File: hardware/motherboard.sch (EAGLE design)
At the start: 66 parts, among them IC1 7805T, Q1 16MHz, U1 ATMEGA328P-PU, U2 L293NE, U3 QRE1113, U4 QRE1113, U5 QRE1113, U6 QRE1113, U7 QRE1113, U8 QRE1113, U9 QRE1113

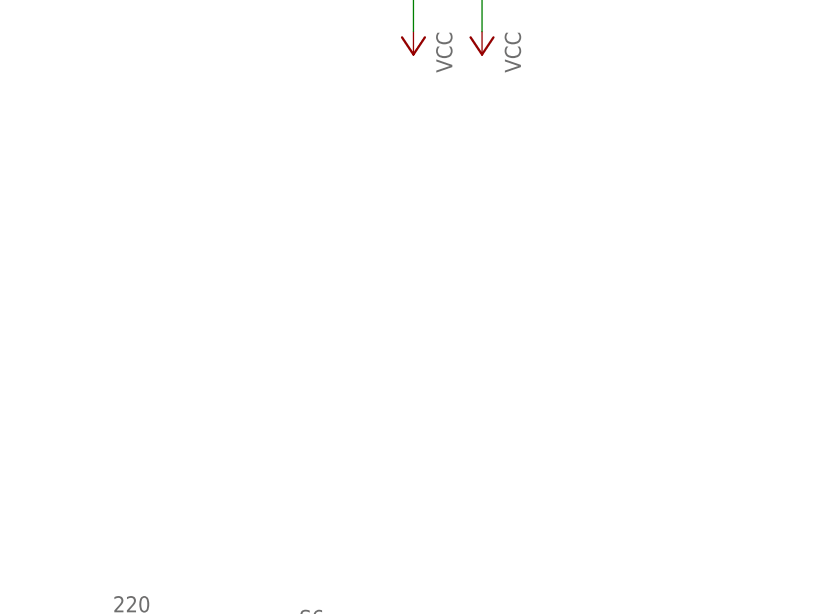
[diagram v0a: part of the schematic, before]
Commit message: Added a new board wich contains sensors.
Modified motherboard and removed sensors. Moved them to a new separate
board.
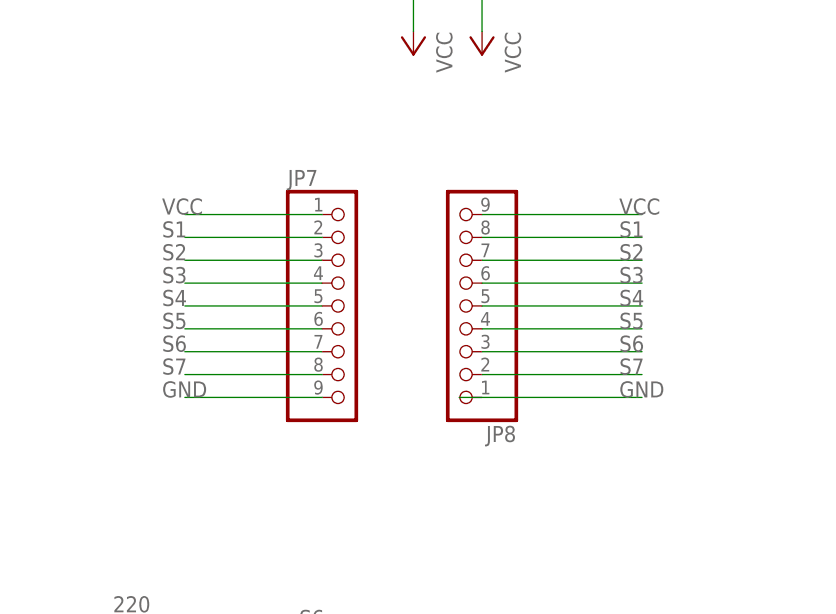
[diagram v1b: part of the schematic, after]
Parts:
- added JP7, JP8: (no value), pinhead:PINHD-1X9
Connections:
- net GND: now also JP7.9
- net S1: now also JP7.2, JP8.8
- net S2: now also JP7.3, JP8.7
- net S3: now also JP7.4, JP8.6
- net S4: now also JP7.5, JP8.5
- net S5: now also JP7.6, JP8.4
- net S6: now also JP7.7, JP8.3
- net S7: now also JP7.8, JP8.2
- net VCC: now also JP7.1, JP8.9
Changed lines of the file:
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@@
 <layers>
 <layer number="1" name="Top" color="4" fill="1" visible="no" active="no"/>
+<layer number="2" name="Route2" color="1" fill="3" visible="no" active="no"/>
+<layer number="3" name="Route3" color="4" fill="3" visible="no" active="no"/>
+<layer number="4" name="Route4" color="1" fill="4" visible="no" active="no"/>
+<layer number="5" name="Route5" color="4" fill="4" visible="no" active="no"/>
+<layer number="6" name="Route6" color="1" fill="8" visible="no" active="no"/>
+<layer number="7" name="Route7" color="4" fill="8" visible="no" active="no"/>
+<layer number="8" name="Route8" color="1" fill="2" visible="no" active="no"/>
+<layer number="9" name="Route9" color="4" fill="2" visible="no" active="no"/>
+<layer number="10" name="Route10" color="1" fill="7" visible="no" active="no"/>
+<layer number="11" name="Route11" color="4" fill="7" visible="no" active="no"/>
+<layer number="12" name="Route12" color="1" fill="5" visible="no" active="no"/>
+<layer number="13" name="Route13" color="4" fill="5" visible="no" active="no"/>
+<layer number="14" name="Route14" color="1" fill="6" visible="no" active="no"/>
+<layer number="15" name="Route15" color="4" fill="6" visible="no" active="no"/>
 <layer number="16" name="Bottom" color="1" fill="1" visible="no" active="no"/>
 <layer number="17" name="Pads" color="2" fill="1" visible="no" active="no"/>
@@
 <part name="R22" library="resistor" deviceset="R-EU_" device="M0805" value="10K"/>
 <part name="R23" library="resistor" deviceset="R-EU_" device="M0805" value="10K"/>
+<part name="JP7" library="pinhead" deviceset="PINHD-1X9" device=""/>
+<part name="JP8" library="pinhead" deviceset="PINHD-1X9" device=""/>
 </parts>
 <sheets>
@@
 <instance part="R22" gate="G$1" x="154.94" y="73.66" rot="R90"/>
 <instance part="R23" gate="G$1" x="144.78" y="73.66" rot="R90"/>
+<instance part="JP7" gate="A" x="726.44" y="86.36"/>
+<instance part="JP8" gate="A" x="739.14" y="86.36" rot="R180"/>
 </instances>
 <busses>
@@
 <wire x1="165.1" y1="40.64" x2="165.1" y2="43.18" width="0.1524" layer="91"/>
 </segment>
+<segment>
+<pinref part="JP7" gate="A" pin="9"/>
+<wire x1="723.9" y1="76.2" x2="708.66" y2="76.2" width="0.1524" layer="91"/>
+<label x="706.12" y="76.2" size="1.778" layer="95"/>
+</segment>
+<segment>
+<wire x1="739.14" y1="76.2" x2="759.46" y2="76.2" width="0.1524" layer="91"/>
+<label x="756.92" y="76.2" size="1.778" layer="95"/>
+</segment>
 </net>
 <net name="VCC" class="0">
@@
 <wire x1="165.1" y1="81.28" x2="165.1" y2="78.74" width="0.1524" layer="91"/>
 </segment>
+<segment>
+<pinref part="JP7" gate="A" pin="1"/>
+<wire x1="723.9" y1="96.52" x2="708.66" y2="96.52" width="0.1524" layer="91"/>
+<label x="706.12" y="96.52" size="1.778" layer="95"/>
+</segment>
+<segment>
+<pinref part="JP8" gate="A" pin="9"/>
+<wire x1="741.68" y1="96.52" x2="759.46" y2="96.52" width="0.1524" layer="91"/>
+<label x="756.92" y="96.52" size="1.778" layer="95"/>
+</segment>
 </net>
 <net name="RESET" class="0">
@@
 <label x="246.38" y="157.48" size="1.778" layer="95"/>
 </segment>
+<segment>
+<pinref part="JP7" gate="A" pin="2"/>
+<wire x1="723.9" y1="93.98" x2="708.66" y2="93.98" width="0.1524" layer="91"/>
+<label x="706.12" y="93.98" size="1.778" layer="95"/>
+</segment>
+<segment>
+<pinref part="JP8" gate="A" pin="8"/>
+<wire x1="741.68" y1="93.98" x2="759.46" y2="93.98" width="0.1524" layer="91"/>
+<label x="756.92" y="93.98" size="1.778" layer="95"/>
+</segment>
 </net>
 <net name="N$9" class="0">
@@
 <label x="246.38" y="154.94" size="1.778" layer="95"/>
 </segment>
+<segment>
+<pinref part="JP7" gate="A" pin="3"/>
+<wire x1="723.9" y1="91.44" x2="708.66" y2="91.44" width="0.1524" layer="91"/>
+<label x="706.12" y="91.44" size="1.778" layer="95"/>
+</segment>
+<segment>
+<pinref part="JP8" gate="A" pin="7"/>
+<wire x1="741.68" y1="91.44" x2="759.46" y2="91.44" width="0.1524" layer="91"/>
+<label x="756.92" y="91.44" size="1.778" layer="95"/>
+</segment>
 </net>
 <net name="S3" class="0">
@@
 <label x="246.38" y="152.4" size="1.778" layer="95"/>
 </segment>
+<segment>
+<pinref part="JP7" gate="A" pin="4"/>
+<wire x1="723.9" y1="88.9" x2="708.66" y2="88.9" width="0.1524" layer="91"/>
+<label x="706.12" y="88.9" size="1.778" layer="95"/>
+</segment>
+<segment>
+<pinref part="JP8" gate="A" pin="6"/>
+<wire x1="741.68" y1="88.9" x2="759.46" y2="88.9" width="0.1524" layer="91"/>
+<label x="756.92" y="88.9" size="1.778" layer="95"/>
+</segment>
 </net>
 <net name="S4" class="0">
@@
 <label x="246.38" y="149.86" size="1.778" layer="95"/>
 </segment>
+<segment>
+<pinref part="JP7" gate="A" pin="5"/>
+<wire x1="723.9" y1="86.36" x2="708.66" y2="86.36" width="0.1524" layer="91"/>
+<label x="706.12" y="86.36" size="1.778" layer="95"/>
+</segment>
+<segment>
+<pinref part="JP8" gate="A" pin="5"/>
+<wire x1="741.68" y1="86.36" x2="759.46" y2="86.36" width="0.1524" layer="91"/>
+<label x="756.92" y="86.36" size="1.778" layer="95"/>
+</segment>
 </net>
 <net name="S5" class="0">
@@
 <label x="246.38" y="144.78" size="1.778" layer="95"/>
 </segment>
+<segment>
+<pinref part="JP7" gate="A" pin="6"/>
+<wire x1="723.9" y1="83.82" x2="708.66" y2="83.82" width="0.1524" layer="91"/>
+<label x="706.12" y="83.82" size="1.778" layer="95"/>
+</segment>
+<segment>
+<pinref part="JP8" gate="A" pin="4"/>
+<wire x1="741.68" y1="83.82" x2="759.46" y2="83.82" width="0.1524" layer="91"/>
+<label x="756.92" y="83.82" size="1.778" layer="95"/>
+</segment>
 </net>
 <net name="S6" class="0">
@@
 <label x="246.38" y="134.62" size="1.778" layer="95"/>
 </segment>
+<segment>
+<pinref part="JP7" gate="A" pin="7"/>
+<wire x1="723.9" y1="81.28" x2="708.66" y2="81.28" width="0.1524" layer="91"/>
+<label x="706.12" y="81.28" size="1.778" layer="95"/>
+</segment>
+<segment>
+<pinref part="JP8" gate="A" pin="3"/>
+<wire x1="741.68" y1="81.28" x2="759.46" y2="81.28" width="0.1524" layer="91"/>
+<label x="756.92" y="81.28" size="1.778" layer="95"/>
+</segment>
 </net>
 <net name="S7" class="0">
@@
 <label x="246.38" y="132.08" size="1.778" layer="95"/>
 </segment>
-</net>
+<segment>
+<pinref part="JP7" gate="A" pin="8"/>
+<wire x1="723.9" y1="78.74" x2="708.66" y2="78.74" width="0.1524" layer="91"/>
+<label x="706.12" y="78.74" size="1.778" layer="95"/>
+</segment>
+<segment>
+<pinref part="JP8" gate="A" pin="2"/>
+<wire x1="741.68" y1="78.74" x2="759.46" y2="78.74" width="0.1524" layer="91"/>
+<label x="756.92" y="78.74" size="1.778" layer="95"/>
+</segment>
+</net>

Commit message: Added pin header to motherboard. Fixed all wire connection from motherboard.
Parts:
- removed JP8: (no value), pinhead:PINHD-1X9
- removed R10, R12, R14, R16, R4, R6, R8: 100, resistor:R-EU_M0805
- removed R11, R13, R15, R17, R5, R7, R9: 220, resistor:R-EU_M0805
- removed U3, U4, U5, U6, U7, U8, U9: QRE1113, SparkFun-Sensors:QRE1113
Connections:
- removed net N$10: R8.2, U4.A
- removed net N$11: R10.2, U5.A
- removed net N$12: R12.2, U6.A
- removed net N$13: R14.2, U8.A
- removed net N$14: R16.2, U9.A
- removed net N$8: R4.2, U7.A
- removed net N$9: R6.2, U3.A
- net GND: now also JP7.1; no longer JP7.9, U3.E, U3.K, U4.E, U4.K, U5.E, U5.K, U6.E, U6.K, U7.E, U7.K, U8.E, U8.K, U9.E, U9.K
- net S1: now also JP7.8; no longer JP7.2, JP8.8, R5.1
- net S2: now also JP7.7; no longer JP7.3, JP8.7, R7.1
- net S3: now also JP7.6; no longer JP7.4, JP8.6, R11.1
- net S4: no longer JP8.5, R9.1
- net S5: now also JP7.4; no longer JP7.6, JP8.4, R13.1
- net S6: now also JP7.3; no longer JP7.7, JP8.3, R15.1
- net S7: now also JP7.2; no longer JP7.8, JP8.2, R17.1
- net VCC: now also JP7.9; no longer JP7.1, JP8.9, R10.1, R11.2, R12.1, R13.2, R14.1, R15.2, R16.1, R17.2, R4.1, R5.2, R6.1, R7.2, R8.1, R9.2, U3.C, U4.C, U5.C, U6.C, U7.C, U8.C, U9.C
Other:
- moved on the sheet: JP7

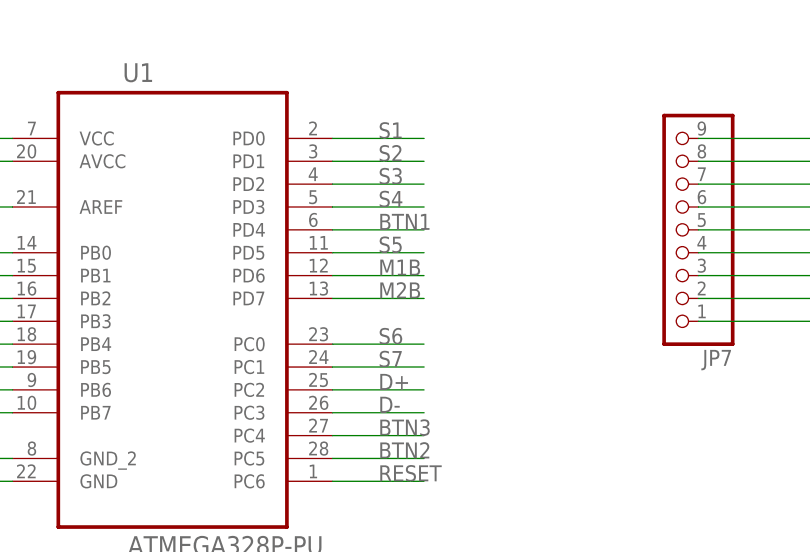
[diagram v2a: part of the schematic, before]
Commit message: Added capacitors to sensor board. Fixed routing.
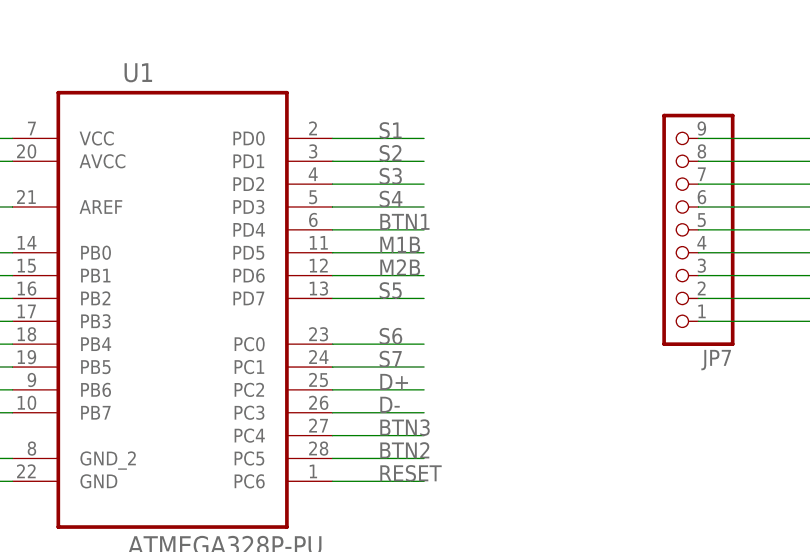
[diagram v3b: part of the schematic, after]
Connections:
- net M1B: now also U1.PD5; no longer U1.PD6
- net M2B: now also U1.PD6; no longer U1.PD7
- net S5: now also U1.PD7; no longer U1.PD5
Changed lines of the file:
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@@
 </segment>
 <segment>
-<pinref part="U1" gate="A" pin="PD6"/>
-<wire x1="241.3" y1="142.24" x2="251.46" y2="142.24" width="0.1524" layer="91"/>
-<label x="246.38" y="142.24" size="1.778" layer="95"/>
+<pinref part="U1" gate="A" pin="PD5"/>
+<wire x1="241.3" y1="144.78" x2="251.46" y2="144.78" width="0.1524" layer="91"/>
+<label x="246.38" y="144.78" size="1.778" layer="95"/>
 </segment>
 </net>
@@
 </segment>
 <segment>
-<pinref part="U1" gate="A" pin="PD7"/>
-<wire x1="241.3" y1="139.7" x2="251.46" y2="139.7" width="0.1524" layer="91"/>
-<label x="246.38" y="139.7" size="1.778" layer="95"/>
+<pinref part="U1" gate="A" pin="PD6"/>
+<wire x1="241.3" y1="142.24" x2="251.46" y2="142.24" width="0.1524" layer="91"/>
+<label x="246.38" y="142.24" size="1.778" layer="95"/>
 </segment>
 </net>
@@
 <net name="S5" class="0">
 <segment>
-<pinref part="U1" gate="A" pin="PD5"/>
-<wire x1="241.3" y1="144.78" x2="251.46" y2="144.78" width="0.1524" layer="91"/>
-<label x="246.38" y="144.78" size="1.778" layer="95"/>
-</segment>
-<segment>
 <pinref part="JP7" gate="A" pin="4"/>
 <wire x1="281.94" y1="144.78" x2="297.18" y2="144.78" width="0.1524" layer="91"/>
 <label x="294.64" y="144.78" size="1.778" layer="95"/>
 </segment>
+<segment>
+<pinref part="U1" gate="A" pin="PD7"/>
+<wire x1="241.3" y1="139.7" x2="251.46" y2="139.7" width="0.1524" layer="91"/>
+<label x="246.38" y="139.7" size="1.778" layer="95"/>
+</segment>
 </net>

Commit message: Fixed motherboard errors.
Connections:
- net VCC: no longer D1.C, D2.C, D3.C, D4.C
- net VCC/2: now also D1.C, D2.C, D3.C, D4.C
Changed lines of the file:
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@@
 <?xml version="1.0" encoding="utf-8"?>
 <!DOCTYPE eagle SYSTEM "eagle.dtd">
-<eagle version="7.5.0">
+<eagle version="7.6.0">
 <drawing>
 <settings>
@@
 <setting verticaltext="up"/>
 </settings>
-<grid distance="0.1" unitdist="inch" unit="inch" style="lines" multiple="1" display="no" altdistance="0.01" altunitdist="inch" altunit="inch"/>
+<grid distance="0.1" unitdist="inch" unit="inch" style="lines" multiple="1" display="yes" altdistance="0.05" altunitdist="inch" altunit="inch"/>
 <layers>
 <layer number="1" name="Top" color="4" fill="1" visible="no" active="no"/>
@@
 <pinref part="U2" gate="A" pin="VCC2"/>
 <pinref part="P+7" gate="G$1" pin="VCC/2"/>
-<wire x1="373.38" y1="104.14" x2="355.6" y2="104.14" width="0.1524" layer="91"/>
+<wire x1="373.38" y1="104.14" x2="365.76" y2="104.14" width="0.1524" layer="91"/>
+<wire x1="365.76" y1="104.14" x2="355.6" y2="104.14" width="0.1524" layer="91"/>
 <wire x1="355.6" y1="104.14" x2="355.6" y2="114.3" width="0.1524" layer="91"/>
 <pinref part="C8" gate="G$1" pin="2"/>
 <wire x1="350.52" y1="104.14" x2="355.6" y2="104.14" width="0.1524" layer="91"/>
 <junction x="355.6" y="104.14"/>
+<wire x1="414.02" y1="124.46" x2="414.02" y2="139.7" width="0.1524" layer="91"/>
+<wire x1="414.02" y1="139.7" x2="365.76" y2="139.7" width="0.1524" layer="91"/>
+<wire x1="421.64" y1="124.46" x2="421.64" y2="139.7" width="0.1524" layer="91"/>
+<wire x1="421.64" y1="139.7" x2="414.02" y2="139.7" width="0.1524" layer="91"/>
+<junction x="414.02" y="139.7"/>
+<pinref part="D3" gate="1" pin="C"/>
+<wire x1="429.26" y1="124.46" x2="429.26" y2="139.7" width="0.1524" layer="91"/>
+<wire x1="429.26" y1="139.7" x2="421.64" y2="139.7" width="0.1524" layer="91"/>
+<junction x="421.64" y="139.7"/>
+<pinref part="D4" gate="1" pin="C"/>
+<wire x1="436.88" y1="124.46" x2="436.88" y2="139.7" width="0.1524" layer="91"/>
+<wire x1="436.88" y1="139.7" x2="429.26" y2="139.7" width="0.1524" layer="91"/>
+<junction x="429.26" y="139.7"/>
+<pinref part="D1" gate="1" pin="C"/>
+<pinref part="D2" gate="1" pin="C"/>
+<wire x1="365.76" y1="139.7" x2="365.76" y2="104.14" width="0.1524" layer="91"/>
+<junction x="365.76" y="104.14"/>
 </segment>
 </net>
@@
 </segment>
 <segment>
+<pinref part="P+6" gate="VCC" pin="VCC"/>
 <pinref part="U2" gate="A" pin="VCC1"/>
-<wire x1="373.38" y1="106.68" x2="365.76" y2="106.68" width="0.1524" layer="91"/>
-<pinref part="P+6" gate="VCC" pin="VCC"/>
-<wire x1="365.76" y1="106.68" x2="360.68" y2="106.68" width="0.1524" layer="91"/>
+<wire x1="373.38" y1="106.68" x2="360.68" y2="106.68" width="0.1524" layer="91"/>
 <wire x1="360.68" y1="106.68" x2="360.68" y2="116.84" width="0.1524" layer="91"/>
-<pinref part="C9" gate="G$1" pin="2"/>
-<wire x1="342.9" y1="104.14" x2="342.9" y2="106.68" width="0.1524" layer="91"/>
-<wire x1="342.9" y1="106.68" x2="360.68" y2="106.68" width="0.1524" layer="91"/>
 <junction x="360.68" y="106.68"/>
 <pinref part="U2" gate="A" pin="1,2EN"/>
 <wire x1="373.38" y1="99.06" x2="360.68" y2="99.06" width="0.1524" layer="91"/>
-<wire x1="360.68" y1="99.06" x2="360.68" y2="106.68" width="0.1524" layer="91"/>
 <pinref part="U2" gate="A" pin="3,4EN"/>
 <wire x1="373.38" y1="96.52" x2="360.68" y2="96.52" width="0.1524" layer="91"/>
 <wire x1="360.68" y1="96.52" x2="360.68" y2="99.06" width="0.1524" layer="91"/>
 <junction x="360.68" y="99.06"/>
-<wire x1="414.02" y1="124.46" x2="414.02" y2="139.7" width="0.1524" layer="91"/>
-<wire x1="414.02" y1="139.7" x2="365.76" y2="139.7" width="0.1524" layer="91"/>
-<wire x1="365.76" y1="139.7" x2="365.76" y2="106.68" width="0.1524" layer="91"/>
-<junction x="365.76" y="106.68"/>
-<wire x1="421.64" y1="124.46" x2="421.64" y2="139.7" width="0.1524" layer="91"/>
-<wire x1="421.64" y1="139.7" x2="414.02" y2="139.7" width="0.1524" layer="91"/>
-<junction x="414.02" y="139.7"/>
-<pinref part="D3" gate="1" pin="C"/>
-<wire x1="429.26" y1="124.46" x2="429.26" y2="139.7" width="0.1524" layer="91"/>
-<wire x1="429.26" y1="139.7" x2="421.64" y2="139.7" width="0.1524" layer="91"/>
-<junction x="421.64" y="139.7"/>
-<pinref part="D4" gate="1" pin="C"/>
-<wire x1="436.88" y1="124.46" x2="436.88" y2="139.7" width="0.1524" layer="91"/>
-<wire x1="436.88" y1="139.7" x2="429.26" y2="139.7" width="0.1524" layer="91"/>
-<junction x="429.26" y="139.7"/>
-<pinref part="D1" gate="1" pin="C"/>
-<pinref part="D2" gate="1" pin="C"/>
-</segment>
-<segment>
+<wire x1="360.68" y1="99.06" x2="360.68" y2="106.68" width="0.1524" layer="91"/>
+<wire x1="342.9" y1="106.68" x2="360.68" y2="106.68" width="0.1524" layer="91"/>
+<pinref part="C9" gate="G$1" pin="2"/>
+<wire x1="342.9" y1="104.14" x2="342.9" y2="106.68" width="0.1524" layer="91"/>
+</segment>
+<segment>
